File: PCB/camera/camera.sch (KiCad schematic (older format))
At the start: 16 parts, among them J1 Conn_01x02, J2 Conn_01x04, J3 Conn_01x02, U1 NRF24L01_Breakout, U2 LM7805

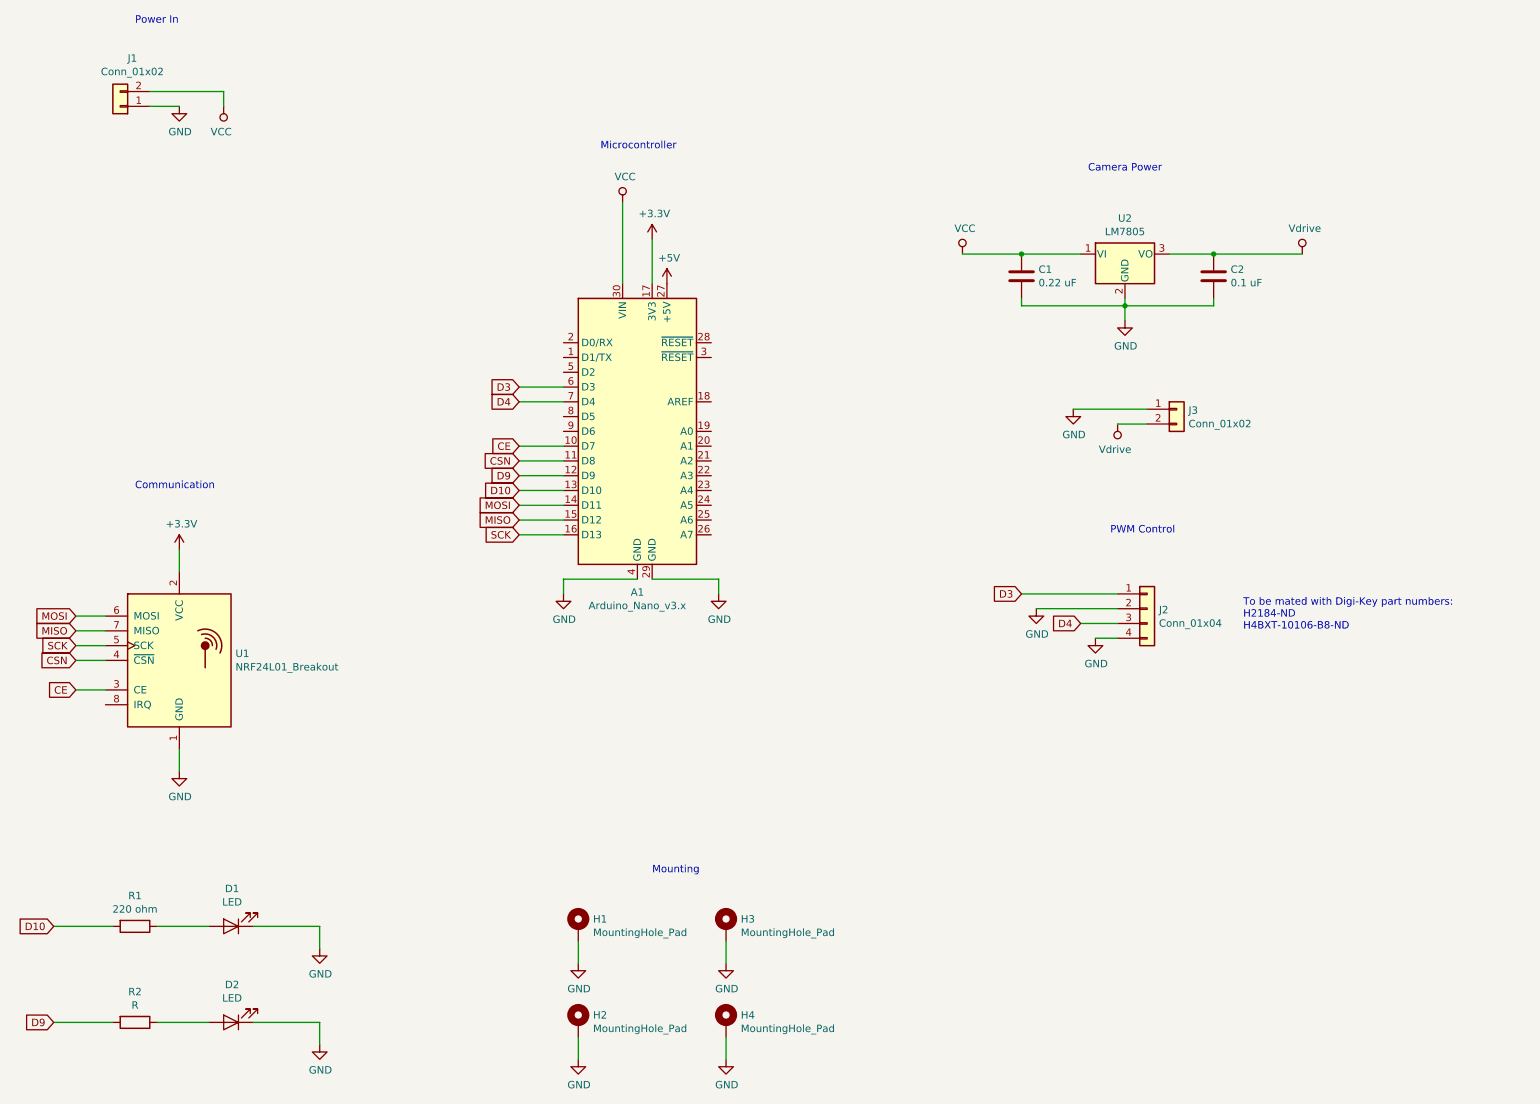
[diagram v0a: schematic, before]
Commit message: Completed camera layout
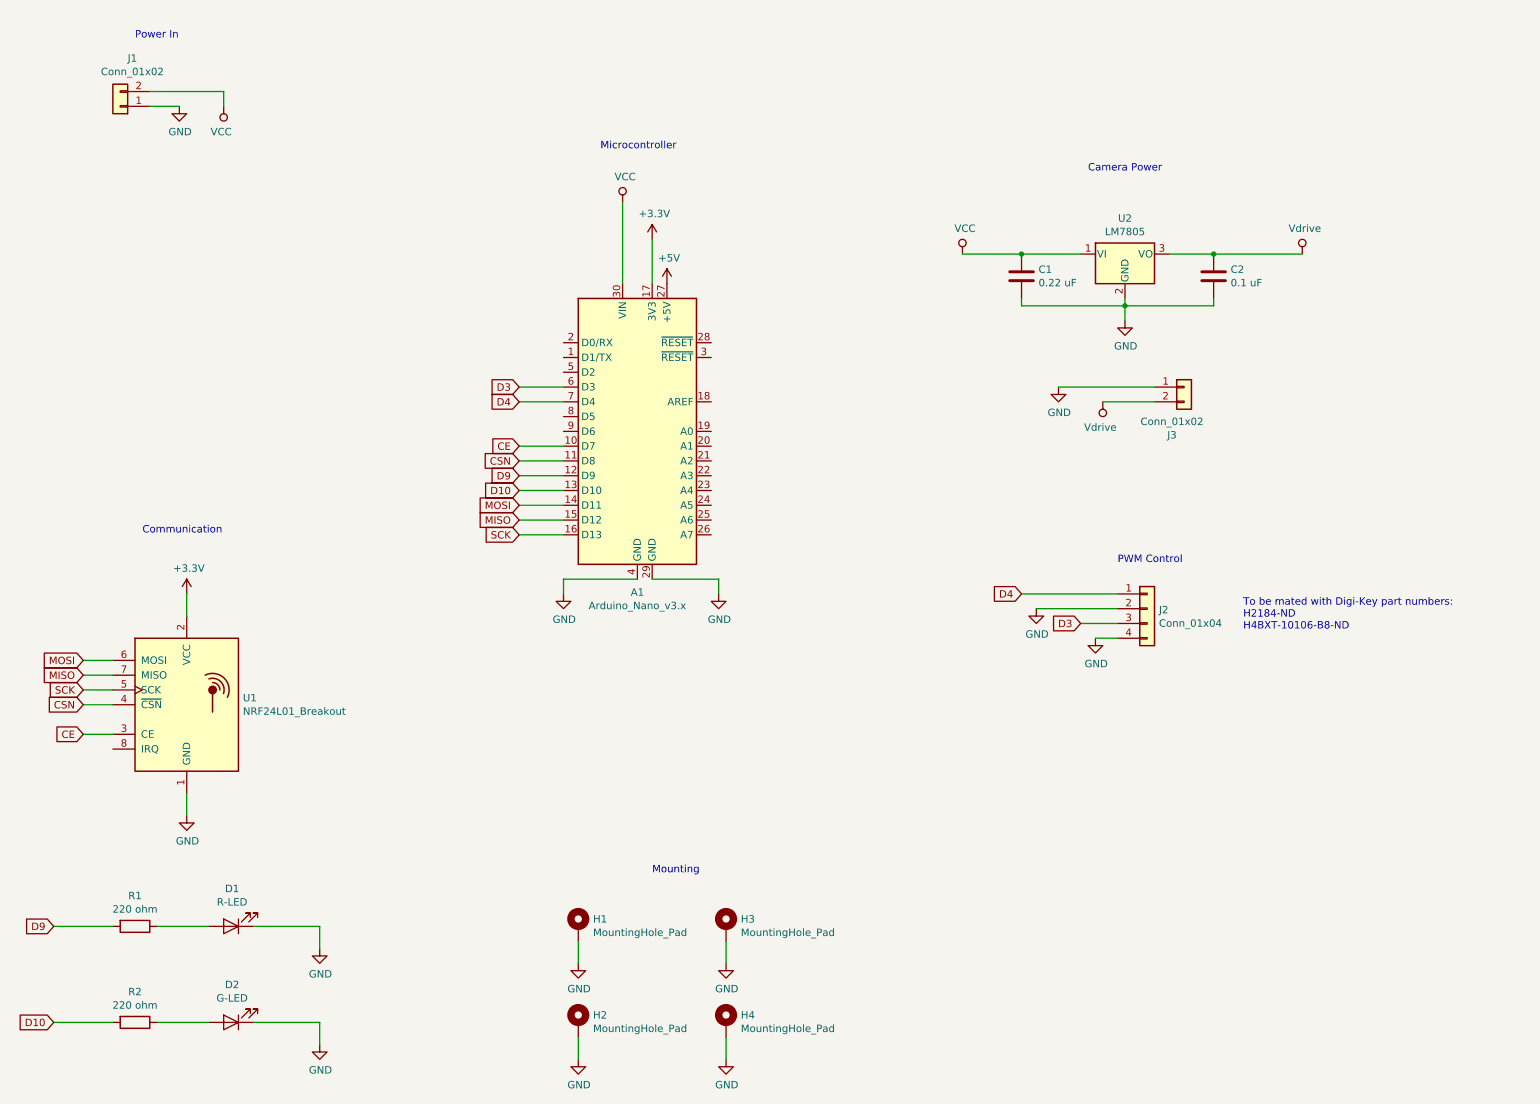
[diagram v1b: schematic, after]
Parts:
- C1: Field4 (none) -> 445-7409-1-ND
- C2: Field4 (none) -> 399-7845-1-ND
- D1: value LED -> R-LED; Field4 (none) -> 160-1447-1-ND
- D2: value LED -> G-LED; Field4 (none) -> 160-1443-6-ND
- J1, J3: Field4 (none) -> WM1860-ND
- J2: Field4 (none) -> WM1862-ND
- R1: Field4 (none) -> P220BZCT-ND
- R2: value R -> 220 ohm; Field4 (none) -> P220BZCT-ND
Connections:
- net D10: now also R2.2; no longer R1.2
- net D3: now also J2.3 (Pin_3); no longer J2.1 (Pin_1)
- net D4: now also J2.1 (Pin_1); no longer J2.3 (Pin_3)
- net D9: now also R1.2; no longer R2.2
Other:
- moved on the sheet: U1
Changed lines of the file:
@@
 encoding utf-8
 Sheet 1 1
-Title ""
-Date "2020-05-06"
+Title "Camera"
+Date "2020-05-07"
 Rev "1"
-Comp ""
+Comp "Mark Sherstan"
 Comment1 ""
 Comment2 ""
@@
 L RF:NRF24L01_Breakout U1
 U 1 1 5EB37153
-P 1700 5100
-F 0 "U1" H 2080 5146 50  0000 L CNN
-F 1 "NRF24L01_Breakout" H 2080 5055 50  0000 L CNN
-F 2 "RF_Module:nRF24L01_Breakout" H 1850 5700 50  0001 L CIN
-F 3 "http://www.nordicsemi.com/eng/content/download/2730/34105/file/nRF24L01_Product_Specification_v2_0.pdf" H 1700 5000 50  0001 C CNN
-	1    1700 5100
+P 1750 5400
+F 0 "U1" H 2130 5446 50  0000 L CNN
+F 1 "NRF24L01_Breakout" H 2130 5355 50  0000 L CNN
+F 2 "RF_Module:nRF24L01_Breakout" H 1900 6000 50  0001 L CIN
+F 3 "http://www.nordicsemi.com/eng/content/download/2730/34105/file/nRF24L01_Product_Specification_v2_0.pdf" H 1750 5300 50  0001 C CNN
+	1    1750 5400
 	1    0    0    -1
 $EndComp
@@
 L power:GND #PWR0106
 U 1 1 5EB3CD7B
-P 1700 5850
-F 0 "#PWR0106" H 1700 5600 50  0001 C CNN
-F 1 "GND" H 1705 5677 50  0000 C CNN
-F 2 "" H 1700 5850 50  0001 C CNN
-F 3 "" H 1700 5850 50  0001 C CNN
-	1    1700 5850
+P 1750 6150
+F 0 "#PWR0106" H 1750 5900 50  0001 C CNN
+F 1 "GND" H 1755 5977 50  0000 C CNN
+F 2 "" H 1750 6150 50  0001 C CNN
+F 3 "" H 1750 6150 50  0001 C CNN
+	1    1750 6150
 	1    0    0    -1
 $EndComp
@@
 L power:+3.3V #PWR0107
 U 1 1 5EB3DDC5
-P 1700 4350
-F 0 "#PWR0107" H 1700 4200 50  0001 C CNN
-F 1 "+3.3V" H 1715 4523 50  0000 C CNN
-F 2 "" H 1700 4350 50  0001 C CNN
-F 3 "" H 1700 4350 50  0001 C CNN
-	1    1700 4350
-	1    0    0    -1
-$EndComp
-Wire Wire Line
-	1700 4500 1700 4350
-Wire Wire Line
-	1700 5850 1700 5700
-Text GLabel 1000 4800 0    50   Input ~ 0
+P 1750 4650
+F 0 "#PWR0107" H 1750 4500 50  0001 C CNN
+F 1 "+3.3V" H 1765 4823 50  0000 C CNN
+F 2 "" H 1750 4650 50  0001 C CNN
+F 3 "" H 1750 4650 50  0001 C CNN
+	1    1750 4650
+	1    0    0    -1
+$EndComp
+Wire Wire Line
+	1750 4800 1750 4650
+Wire Wire Line
+	1750 6150 1750 6000
+Text GLabel 1050 5100 0    50   Input ~ 0
 MOSI
-Text GLabel 1000 4900 0    50   Input ~ 0
+Text GLabel 1050 5200 0    50   Input ~ 0
 MISO
-Text GLabel 1000 5000 0    50   Input ~ 0
+Text GLabel 1050 5300 0    50   Input ~ 0
 SCK
-Text GLabel 1000 5100 0    50   Input ~ 0
+Text GLabel 1050 5400 0    50   Input ~ 0
 CSN
-Text GLabel 1000 5300 0    50   Input ~ 0
+Text GLabel 1050 5600 0    50   Input ~ 0
 CE
 Wire Wire Line
-	1000 4800 1200 4800
-Wire Wire Line
-	1200 4900 1000 4900
-Wire Wire Line
-	1000 5000 1200 5000
-Wire Wire Line
-	1200 5100 1000 5100
-Wire Wire Line
-	1000 5300 1200 5300
+	1050 5100 1250 5100
+Wire Wire Line
+	1250 5200 1050 5200
+Wire Wire Line
+	1050 5300 1250 5300
+Wire Wire Line
+	1250 5400 1050 5400
+Wire Wire Line
+	1050 5600 1250 5600
 $Comp
 L Device:R R1
@@
 F 1 "220 ohm" V 1284 6900 50  0000 C CNN
 F 2 "Resistor_SMD:R_0603_1608Metric_Pad1.05x0.95mm_HandSolder" V 1330 6900 50  0001 C CNN
-F 3 "~" H 1400 6900 50  0001 C CNN
+F 3 "https://www.digikey.ca/product-detail/en/panasonic-electronic-components/ERJ-PA3J221V/P220BZCT-ND/5036283" H 1400 6900 50  0001 C CNN
+F 4 "P220BZCT-ND" V 1400 6900 50  0001 C CNN "Field4"
 	1    1400 6900
 	0    1    1    0
@@
 P 2050 6900
 F 0 "D1" H 2043 6645 50  0000 C CNN
-F 1 "LED" H 2043 6736 50  0000 C CNN
+F 1 "R-LED" H 2043 6736 50  0000 C CNN
 F 2 "LED_SMD:LED_0603_1608Metric_Pad1.05x0.95mm_HandSolder" H 2050 6900 50  0001 C CNN
-F 3 "~" H 2050 6900 50  0001 C CNN
+F 3 "https://www.digikey.ca/product-detail/en/lite-on-inc/LTST-C191KRKT/160-1447-1-ND/386836" H 2050 6900 50  0001 C CNN
+F 4 "160-1447-1-ND" H 2050 6900 50  0001 C CNN "Field4"
 	1    2050 6900
 	-1   0    0    1
@@
 	1    0    0    -1
 $EndComp
+Text GLabel 850  6900 0    50   Input ~ 0
+D9
 Text GLabel 850  7550 0    50   Input ~ 0
-D9
-Text GLabel 850  6900 0    50   Input ~ 0
 D10
 Text GLabel 4000 3850 0    50   Input ~ 0
@@
 	2650 6900 2650 7050
 $Comp
-L Device:R R2
-U 1 1 5EB48633
-P 1400 7550
-F 0 "R2" V 1193 7550 50  0000 C CNN
-F 1 "R" V 1284 7550 50  0000 C CNN
-F 2 "Resistor_SMD:R_0603_1608Metric_Pad1.05x0.95mm_HandSolder" V 1330 7550 50  0001 C CNN
-F 3 "~" H 1400 7550 50  0001 C CNN
-	1    1400 7550
-	0    1    1    0
-$EndComp
-$Comp
 L Device:LED D2
 U 1 1 5EB48639
 P 2050 7550
 F 0 "D2" H 2043 7295 50  0000 C CNN
-F 1 "LED" H 2043 7386 50  0000 C CNN
+F 1 "G-LED" H 2043 7386 50  0000 C CNN
 F 2 "LED_SMD:LED_0603_1608Metric_Pad1.05x0.95mm_HandSolder" H 2050 7550 50  0001 C CNN
-F 3 "~" H 2050 7550 50  0001 C CNN
+F 3 "https://www.digikey.ca/product-detail/en/lite-on-inc/LTST-C191GKT/160-1443-6-ND/1888655" H 2050 7550 50  0001 C CNN
+F 4 "160-1443-6-ND" H 2050 7550 50  0001 C CNN "Field4"
 	1    2050 7550
 	-1   0    0    1
@@
 F 1 "Conn_01x02" H 1218 1116 50  0000 C CNN
 F 2 "Connector_Molex:Molex_Micro-Fit_3.0_43650-0200_1x02_P3.00mm_Horizontal" H 1300 1350 50  0001 C CNN
-F 3 "~" H 1300 1350 50  0001 C CNN
+F 3 "https://www.digikey.ca/products/en?keywords=0436500200" H 1300 1350 50  0001 C CNN
+F 4 "WM1860-ND" H 1300 1350 50  0001 C CNN "Field4"
 	1    1300 1350
 	-1   0    0    1
@@
 F 1 "Conn_01x04" H 8330 4651 50  0000 L CNN
 F 2 "Connector_Molex:Molex_Micro-Fit_3.0_43650-0400_1x04_P3.00mm_Horizontal" H 8250 4750 50  0001 C CNN
-F 3 "~" H 8250 4750 50  0001 C CNN
+F 3 "https://www.digikey.ca/products/en?keywords=43650-0400" H 8250 4750 50  0001 C CNN
+F 4 "WM1862-ND" H 8250 4750 50  0001 C CNN "Field4"
 	1    8250 4750
 	1    0    0    -1
@@
 	1    0    0    -1
 $EndComp
+Text GLabel 7400 4650 0    50   Input ~ 0
+D4
 Text GLabel 7800 4850 0    50   Input ~ 0
-D4
-Text GLabel 7400 4650 0    50   Input ~ 0
 D3
 Wire Wire Line
@@
 	1    0    0    -1
 $EndComp
-Text Notes 1400 800  0    50   ~ 0
+Text Notes 1400 900  0    50   ~ 0
 Power In
-Text Notes 1400 3950 0    50   ~ 0
+Text Notes 1450 4250 0    50   ~ 0
 Communication
 Text Notes 4550 1650 0    50   ~ 0
@@
 Text Notes 4900 6550 0    50   ~ 0
 Mounting
-Text Notes 8000 4250 0    50   ~ 0
+Text Notes 8050 4450 0    50   ~ 0
 PWM Control
 Text Notes 7850 1800 0    50   ~ 0
@@
 F 1 "0.22 uF" H 7515 2455 50  0000 L CNN
 F 2 "Capacitor_SMD:C_0603_1608Metric_Pad1.05x0.95mm_HandSolder" H 7438 2350 50  0001 C CNN
-F 3 "~" H 7400 2500 50  0001 C CNN
+F 3 "https://www.digikey.ca/product-detail/en/tdk-corporation/C1608X7R1H224M080AB/445-7409-1-ND/2733481" H 7400 2500 50  0001 C CNN
+F 4 "445-7409-1-ND" H 7400 2500 50  0001 C CNN "Field4"
 	1    7400 2500
 	1    0    0    -1
@@
 F 1 "0.1 uF" H 8815 2455 50  0000 L CNN
 F 2 "Capacitor_SMD:C_0603_1608Metric_Pad1.05x0.95mm_HandSolder" H 8738 2350 50  0001 C CNN
-F 3 "~" H 8700 2500 50  0001 C CNN
+F 3 "https://www.digikey.ca/product-detail/en/kemet/C0603C104M5RACTU/399-7845-1-ND/3471568" H 8700 2500 50  0001 C CNN
+F 4 "399-7845-1-ND" H 8700 2500 50  0001 C CNN "Field4"
 	1    8700 2500
 	1    0    0    -1
@@
 L power:Vdrive #PWR0121
 U 1 1 5EB846CC
-P 8050 3500
-F 0 "#PWR0121" H 7850 3350 50  0001 C CNN
-F 1 "Vdrive" H 8067 3673 50  0000 C CNN
-F 2 "" H 8050 3500 50  0001 C CNN
-F 3 "" H 8050 3500 50  0001 C CNN
-	1    8050 3500
+P 7950 3350
+F 0 "#PWR0121" H 7750 3200 50  0001 C CNN
+F 1 "Vdrive" H 7967 3523 50  0000 C CNN
+F 2 "" H 7950 3350 50  0001 C CNN
+F 3 "" H 7950 3350 50  0001 C CNN
+	1    7950 3350
 	-1   0    0    1
 $EndComp
@@
 L power:GND #PWR0122
 U 1 1 5EB856CF
-P 7750 3400
-F 0 "#PWR0122" H 7750 3150 50  0001 C CNN
-F 1 "GND" H 7755 3227 50  0000 C CNN
-F 2 "" H 7750 3400 50  0001 C CNN
-F 3 "" H 7750 3400 50  0001 C CNN
-	1    7750 3400
-	1    0    0    -1
-$EndComp
-$Comp
-L Connector_Generic:Conn_01x02 J3
-U 1 1 5EB866DC
-P 8450 3400
-F 0 "J3" H 8530 3392 50  0000 L CNN
-F 1 "Conn_01x02" H 8530 3301 50  0000 L CNN
-F 2 "Connector_Molex:Molex_Micro-Fit_3.0_43650-0200_1x02_P3.00mm_Horizontal" H 8450 3400 50  0001 C CNN
-F 3 "~" H 8450 3400 50  0001 C CNN
-	1    8450 3400
-	1    0    0    -1
-$EndComp
-Wire Wire Line
-	7750 3400 8250 3400
-Wire Wire Line
-	8050 3500 8250 3500
+P 7650 3250
+F 0 "#PWR0122" H 7650 3000 50  0001 C CNN
+F 1 "GND" H 7655 3077 50  0000 C CNN
+F 2 "" H 7650 3250 50  0001 C CNN
+F 3 "" H 7650 3250 50  0001 C CNN
+	1    7650 3250
+	1    0    0    -1
+$EndComp
 Text Notes 8900 4900 0    50   ~ 0
 To be mated with Digi-Key part numbers:\nH2184-ND‎\nH4BXT-10106-B8-ND
+$Comp
+L Device:R R2
+U 1 1 5EB92A44
+P 1400 7550
+F 0 "R2" V 1193 7550 50  0000 C CNN
+F 1 "220 ohm" V 1284 7550 50  0000 C CNN
+F 2 "Resistor_SMD:R_0603_1608Metric_Pad1.05x0.95mm_HandSolder" V 1330 7550 50  0001 C CNN
+F 3 "https://www.digikey.ca/product-detail/en/panasonic-electronic-components/ERJ-PA3J221V/P220BZCT-ND/5036283" H 1400 7550 50  0001 C CNN
+F 4 "P220BZCT-ND" V 1400 7550 50  0001 C CNN "Field4"
+	1    1400 7550
+	0    1    1    0
+$EndComp
+$Comp
+L Connector_Generic:Conn_01x02 J3
+U 1 1 5EB98EBE
+P 8500 3250
+F 0 "J3" H 8418 2925 50  0000 C CNN
+F 1 "Conn_01x02" H 8418 3016 50  0000 C CNN
+F 2 "Connector_Molex:Molex_Micro-Fit_3.0_43650-0200_1x02_P3.00mm_Horizontal" H 8500 3250 50  0001 C CNN
+F 3 "https://www.digikey.ca/products/en?keywords=0436500200" H 8500 3250 50  0001 C CNN
+F 4 "WM1860-ND" H 8500 3250 50  0001 C CNN "Field4"
+	1    8500 3250
+	1    0    0    -1
+$EndComp
+Wire Wire Line
+	7650 3250 8300 3250
+Wire Wire Line
+	7950 3350 8300 3350
 $EndSCHEMATC
